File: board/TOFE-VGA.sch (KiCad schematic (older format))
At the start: 6 parts, among them U1 TOFE-8X, U7 24AA01/24LC01B

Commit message: Upgrade schematic
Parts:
- C29: symbol C -> C-RESCUE-TOFE-VGA
- R15, R22: symbol R -> R-RESCUE-TOFE-VGA
- renumbered U1 to U8
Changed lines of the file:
@@
 EESchema Schematic File Version 2
+LIBS:TOFE-VGA-rescue
 LIBS:power
 LIBS:device
@@
 LIBS:EEPROM
 LIBS:TOFE-VGA-cache
-LIBS:TOFE-VGA-cache
-EELAYER 27 0
+EELAYER 25 0
 EELAYER END
 $Descr A3 16535 11693
@@
 $EndDescr
 $Comp
-L TOFE-8X U1
+L TOFE-8X U8
 U 1 1 561CABB0
 P 5450 5200
@@
 $EndComp
 $Comp
-L R R22
+L R-RESCUE-TOFE-VGA R22
 U 1 1 561E30B1
 P 3950 9000
@@
 $EndComp
 $Comp
-L R R15
+L R-RESCUE-TOFE-VGA R15
 U 1 1 561E30BD
 P 3750 9000
@@
 GND
 $Comp
-L C C29
+L C-RESCUE-TOFE-VGA C29
 U 1 1 561E3D38
 P 6000 9900

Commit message: Refactoring for TOFE
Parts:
- removed C29: 0.1uF, ~, symbol C-RESCUE-TOFE-VGA
- removed D4: DIODE, ~, symbol DIODE
- removed R15, R22: 10K, ~, symbol R-RESCUE-TOFE-VGA
- removed U7: 24AA01/24LC01B, ~, symbol 24AA01/24LC01B
- removed U8: TOFE-8X, ~, symbol TOFE-8X
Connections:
- net labels removed: 12V, GND, SCL, SDA, VCC12V, VCC3V3
- wire segments 78 -> 33
- no-connect marks 1 -> 0
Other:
- note removed: "EEPROM"
- note removed: "TOFE-8x"

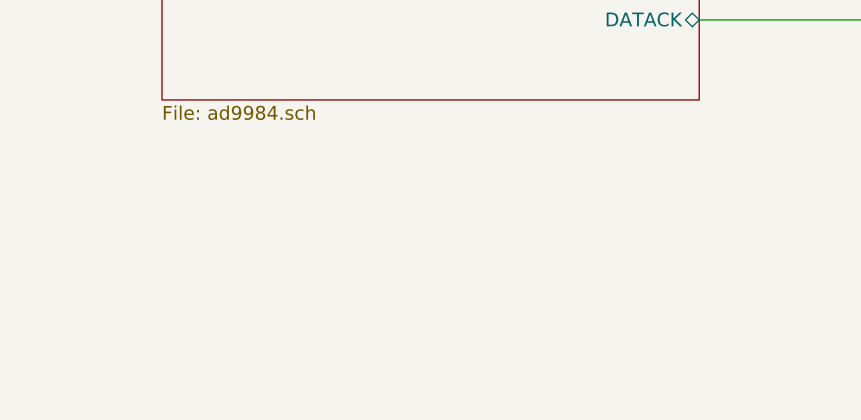
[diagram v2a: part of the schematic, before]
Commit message: Add component inputs for AD9984 secondardy inputs
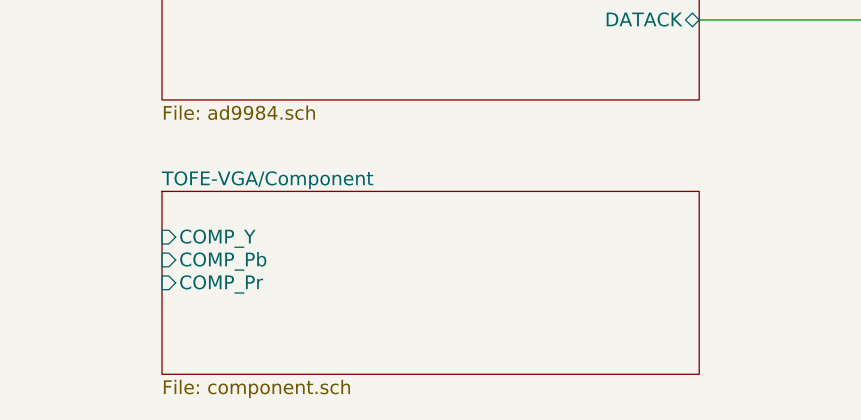
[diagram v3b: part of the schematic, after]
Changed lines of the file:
@@
 $Descr A4 11693 8268
 encoding utf-8
-Sheet 1 5
+Sheet 1 6
 Title "TOFE VGA Expansion Board"
-Date "2015-11-13"
+Date "2015-11-25"
 Rev "1.0"
 Comp "Kenny Duffus <kenny@duffus.org>"
@@
 Wire Bus Line
 	5550 4200 6550 4200
+$Sheet
+S 3200 5900 2350 800
+U 56559E6B
+F0 "TOFE-VGA/Component" 60
+F1 "component.sch" 60
+F2 "COMP_Y" I L 3200 6100 60
+F3 "COMP_Pb" I L 3200 6200 60
+F4 "COMP_Pr" I L 3200 6300 60
+$EndSheet
 $EndSCHEMATC

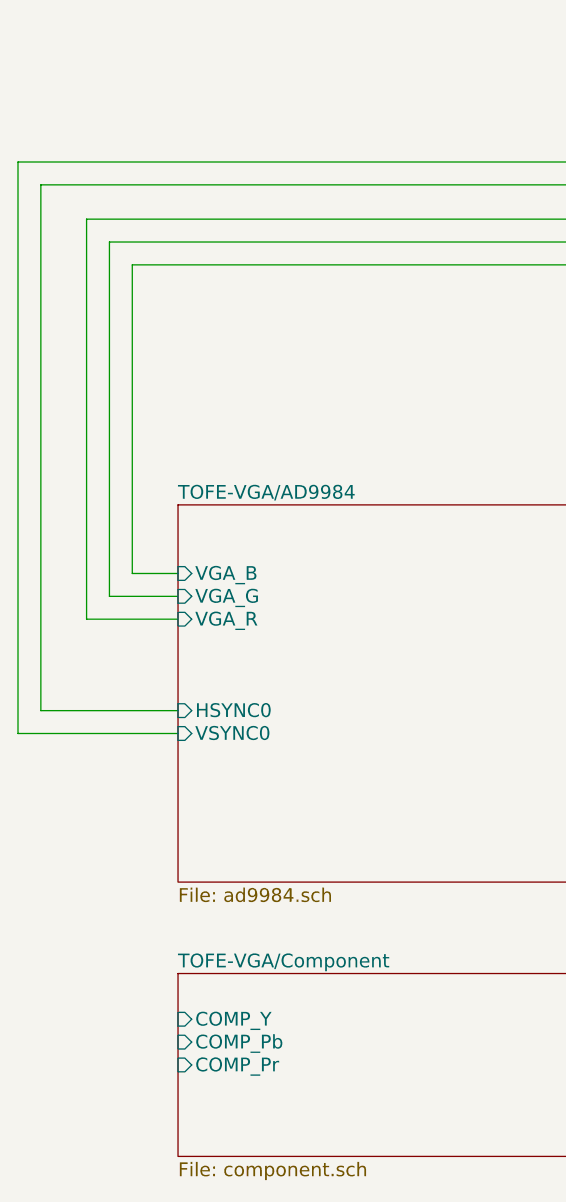
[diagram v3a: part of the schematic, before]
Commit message: Connect component hierarchical pins
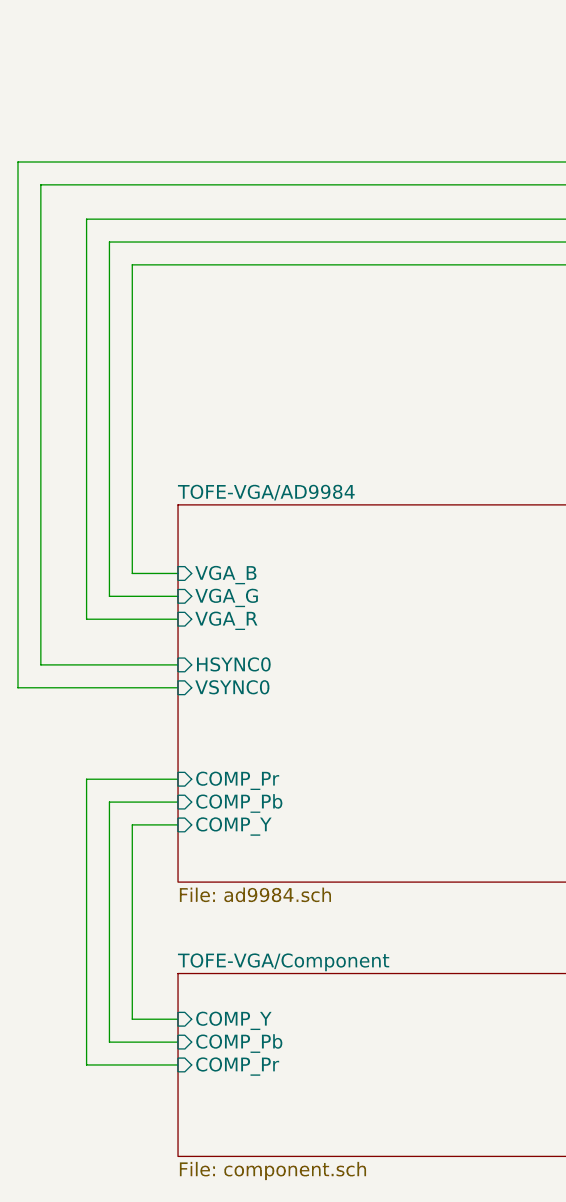
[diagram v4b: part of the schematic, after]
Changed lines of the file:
@@
 Sheet 1 6
 Title "TOFE VGA Expansion Board"
-Date "2015-11-25"
+Date "2016-01-10"
 Rev "1.0"
 Comp "Kenny Duffus <kenny@duffus.org>"
@@
 F9 "SOGOUT" O R 5550 4600 60
 F10 "DATACK" B R 5550 5150 60
-F11 "VSYNC0" I L 3200 4850 60
-F12 "HSYNC0" I L 3200 4750 60
+F11 "VSYNC0" I L 3200 4650 60
+F12 "HSYNC0" I L 3200 4550 60
 F13 "SDA_AD9984" B R 5550 4850 60
 F14 "SCL_AD9984" B R 5550 4950 60
 F15 "VSOUT" O R 5550 4400 60
+F16 "COMP_Y" I L 3200 5250 60
+F17 "COMP_Pb" I L 3200 5150 60
+F18 "COMP_Pr" I L 3200 5050 60
 $EndSheet
 $Sheet
@@
 	2800 4350 2800 2600
 Wire Wire Line
-	2600 2450 2600 4750
-Wire Wire Line
-	2600 4750 3200 4750
-Wire Wire Line
-	3200 4850 2500 4850
-Wire Wire Line
-	2500 4850 2500 2350
-Wire Wire Line
 	5550 4400 6550 4400
 Wire Wire Line
@@
 F4 "COMP_Pr" I L 3200 6300 60
 $EndSheet
+Wire Wire Line
+	3200 4550 2600 4550
+Wire Wire Line
+	2500 4650 3200 4650
+Wire Wire Line
+	2500 2350 2500 4650
+Wire Wire Line
+	2600 4550 2600 2450
+Wire Wire Line
+	3200 5250 3000 5250
+Wire Wire Line
+	3000 5250 3000 6100
+Wire Wire Line
+	3000 6100 3200 6100
+Wire Wire Line
+	3200 6200 2900 6200
+Wire Wire Line
+	2900 6200 2900 5150
+Wire Wire Line
+	2900 5150 3200 5150
+Wire Wire Line
+	3200 5050 2800 5050
+Wire Wire Line
+	2800 5050 2800 6300
+Wire Wire Line
+	2800 6300 3200 6300
 $EndSCHEMATC

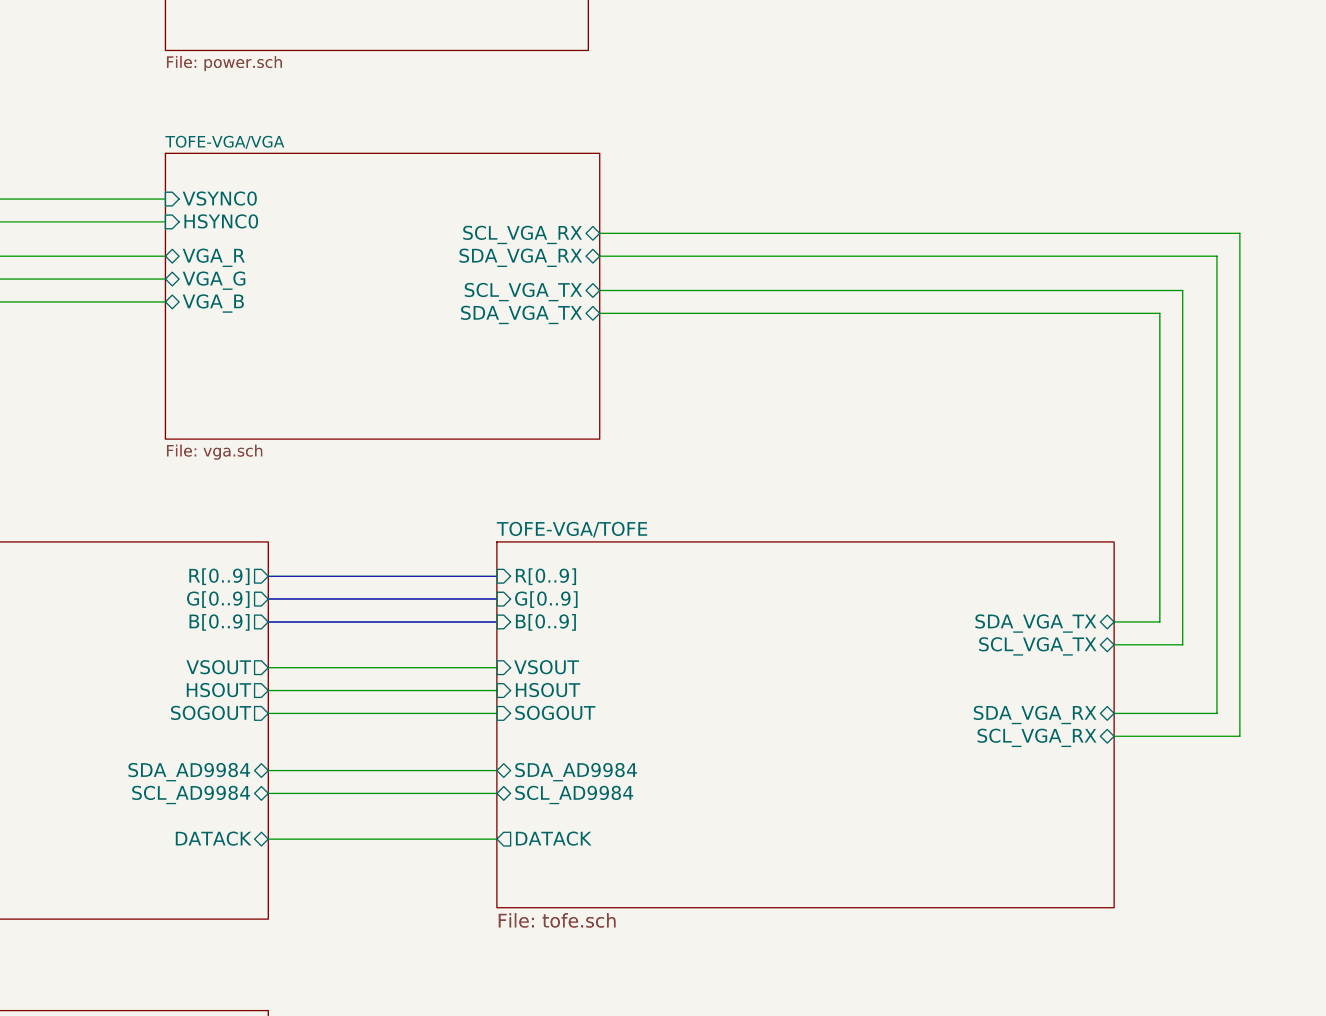
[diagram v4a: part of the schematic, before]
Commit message: Connect I2C level shifter EN to TOFE
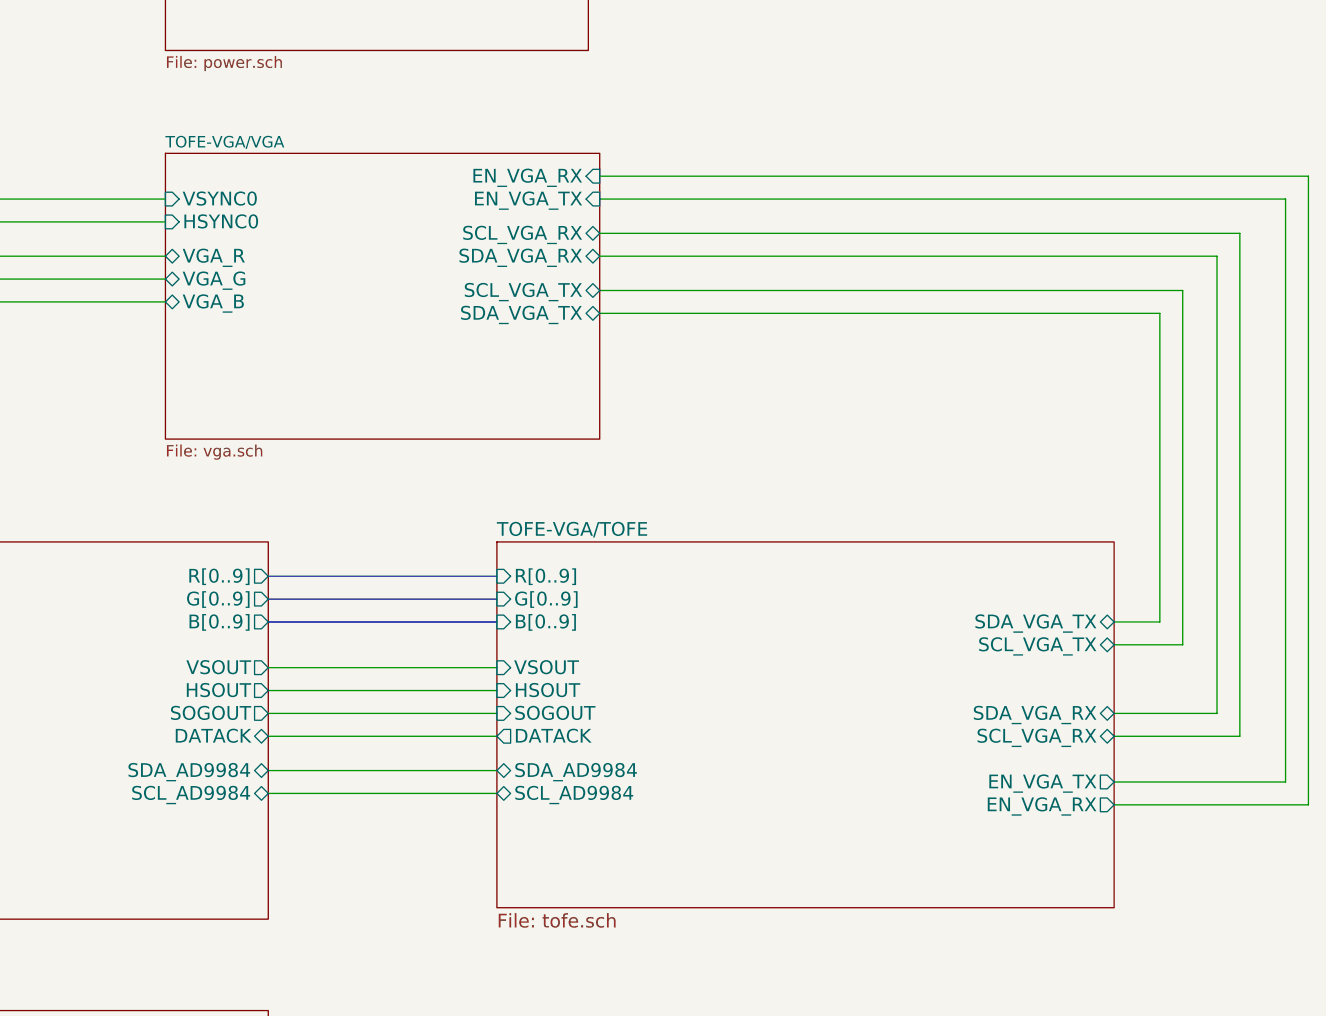
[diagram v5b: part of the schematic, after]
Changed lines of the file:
@@
 F12 "HSOUT" I L 6550 4500 60
 F13 "SOGOUT" I L 6550 4600 60
-F14 "DATACK" O L 6550 5150 60
+F14 "DATACK" O L 6550 4700 60
+F15 "EN_VGA_TX" O R 9250 4900 60
+F16 "EN_VGA_RX" O R 9250 5000 60
 $EndSheet
 $Sheet
@@
 F8 "HSOUT" O R 5550 4500 60
 F9 "SOGOUT" O R 5550 4600 60
-F10 "DATACK" B R 5550 5150 60
+F10 "DATACK" B R 5550 4700 60
 F11 "VSYNC0" I L 3200 4650 60
 F12 "HSYNC0" I L 3200 4550 60
@@
 F9 "HSYNC0" I L 5100 2450 60
 F10 "VSYNC0" I L 5100 2350 60
+F11 "EN_VGA_RX" I R 7000 2250 60
+F12 "EN_VGA_TX" I R 7000 2350 60
 $EndSheet
 Wire Wire Line
@@
 Wire Wire Line
 	5550 4950 6550 4950
-Wire Wire Line
-	5550 5150 6550 5150
 Wire Wire Line
 	3000 2800 5100 2800
@@
 Wire Wire Line
 	2800 6300 3200 6300
+Wire Wire Line
+	5550 4700 6550 4700
+Wire Wire Line
+	7000 2350 10000 2350
+Wire Wire Line
+	10000 2350 10000 4900
+Wire Wire Line
+	10000 4900 9250 4900
+Wire Wire Line
+	9250 5000 10100 5000
+Wire Wire Line
+	10100 5000 10100 2250
+Wire Wire Line
+	10100 2250 7000 2250
 $EndSCHEMATC

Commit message: Lots of small fixes.
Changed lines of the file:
@@
 $Descr A4 11693 8268
 encoding utf-8
-Sheet 1 6
+Sheet 1 5
 Title "TOFE VGA Expansion Board"
 Date "2016-01-10"
@@
 F11 "EN_VGA_RX" I R 7000 2250 60
 F12 "EN_VGA_TX" I R 7000 2350 60
+F13 "COMP_Y" I L 5100 3040 60
+F14 "COMP_Pb" I L 5100 3160 60
+F15 "COMP_Pr" I L 5100 3280 60
 $EndSheet
 Wire Wire Line
@@
 Wire Bus Line
 	5550 4200 6550 4200
-$Sheet
-S 3200 5900 2350 800
-U 56559E6B
-F0 "TOFE-VGA/Component" 60
-F1 "component.sch" 60
-F2 "COMP_Y" I L 3200 6100 60
-F3 "COMP_Pb" I L 3200 6200 60
-F4 "COMP_Pr" I L 3200 6300 60
-$EndSheet
 Wire Wire Line
 	3200 4550 2600 4550
@@
 	2600 4550 2600 2450
 Wire Wire Line
-	3200 5250 3000 5250
+	2150 5250 3200 5250
 Wire Wire Line
-	3000 5250 3000 6100
+	2250 5150 3200 5150
 Wire Wire Line
-	3000 6100 3200 6100
-Wire Wire Line
-	3200 6200 2900 6200
-Wire Wire Line
-	2900 6200 2900 5150
-Wire Wire Line
-	2900 5150 3200 5150
-Wire Wire Line
-	3200 5050 2800 5050
-Wire Wire Line
-	2800 5050 2800 6300
-Wire Wire Line
-	2800 6300 3200 6300
+	2370 5050 3200 5050
 Wire Wire Line
 	5550 4700 6550 4700
@@
 Wire Wire Line
 	10100 2250 7000 2250
+Wire Wire Line
+	2370 5050 2370 3280
+Wire Wire Line
+	2370 3280 5100 3280
+Wire Wire Line
+	2250 5150 2250 3160
+Wire Wire Line
+	2250 3160 5100 3160
+Wire Wire Line
+	2150 5250 2150 3040
+Wire Wire Line
+	2150 3040 5100 3040
 $EndSCHEMATC
